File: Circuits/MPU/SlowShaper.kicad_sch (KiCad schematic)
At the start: 34 parts, among them U22 ADA4805-2ARMZ, U23 ADA4805-2ARMZ

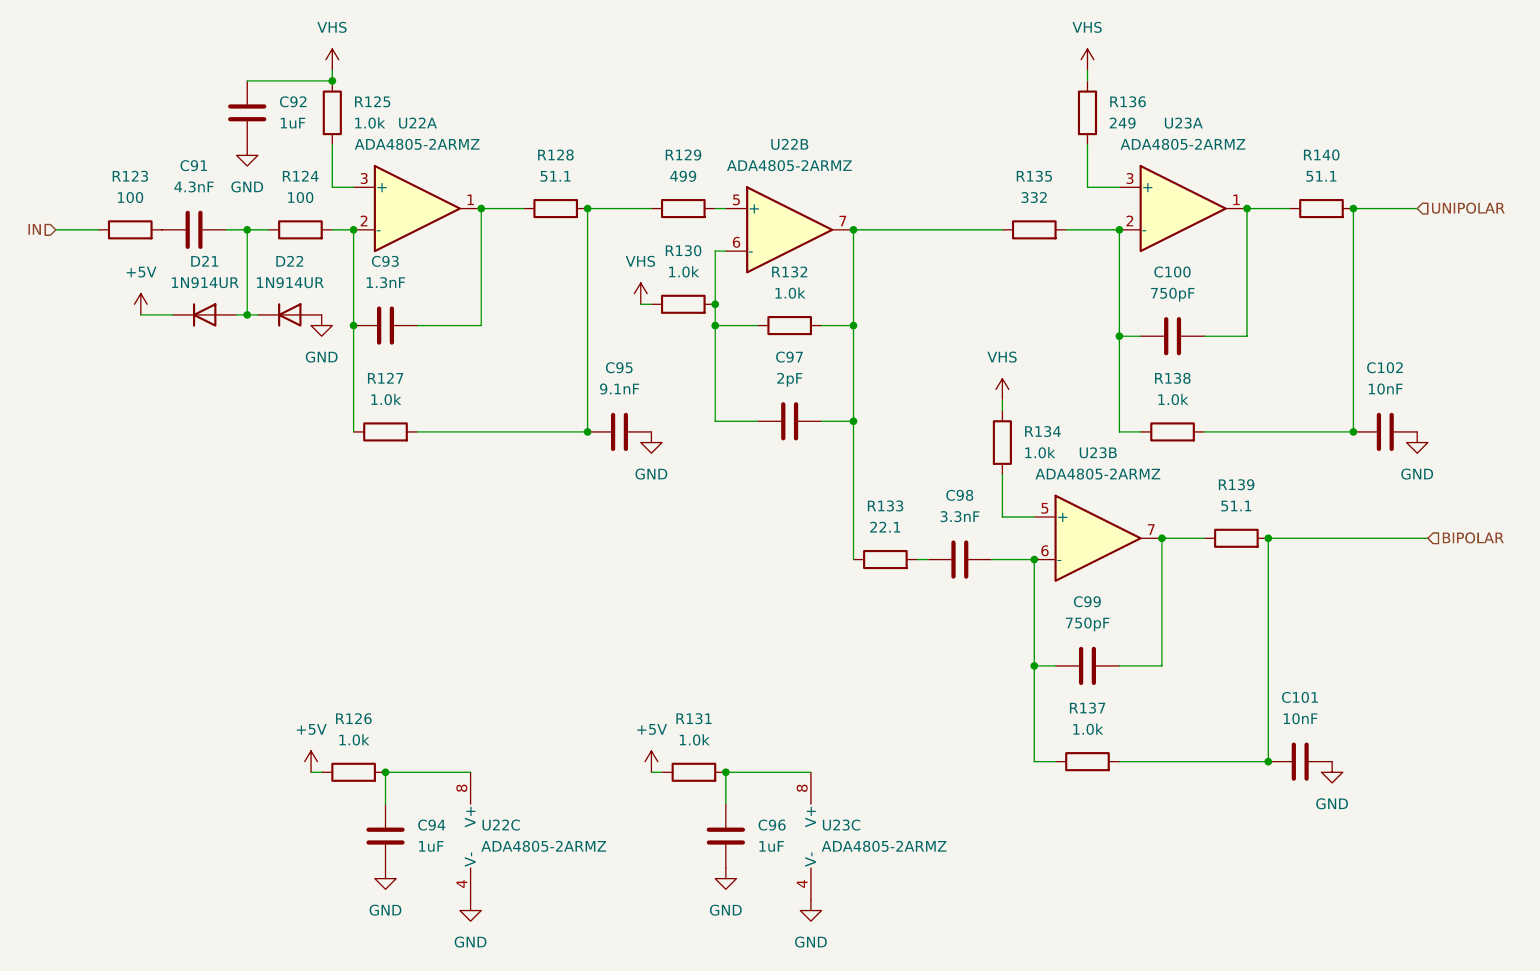
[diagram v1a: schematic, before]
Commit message: PPS is RS422, add MXINH
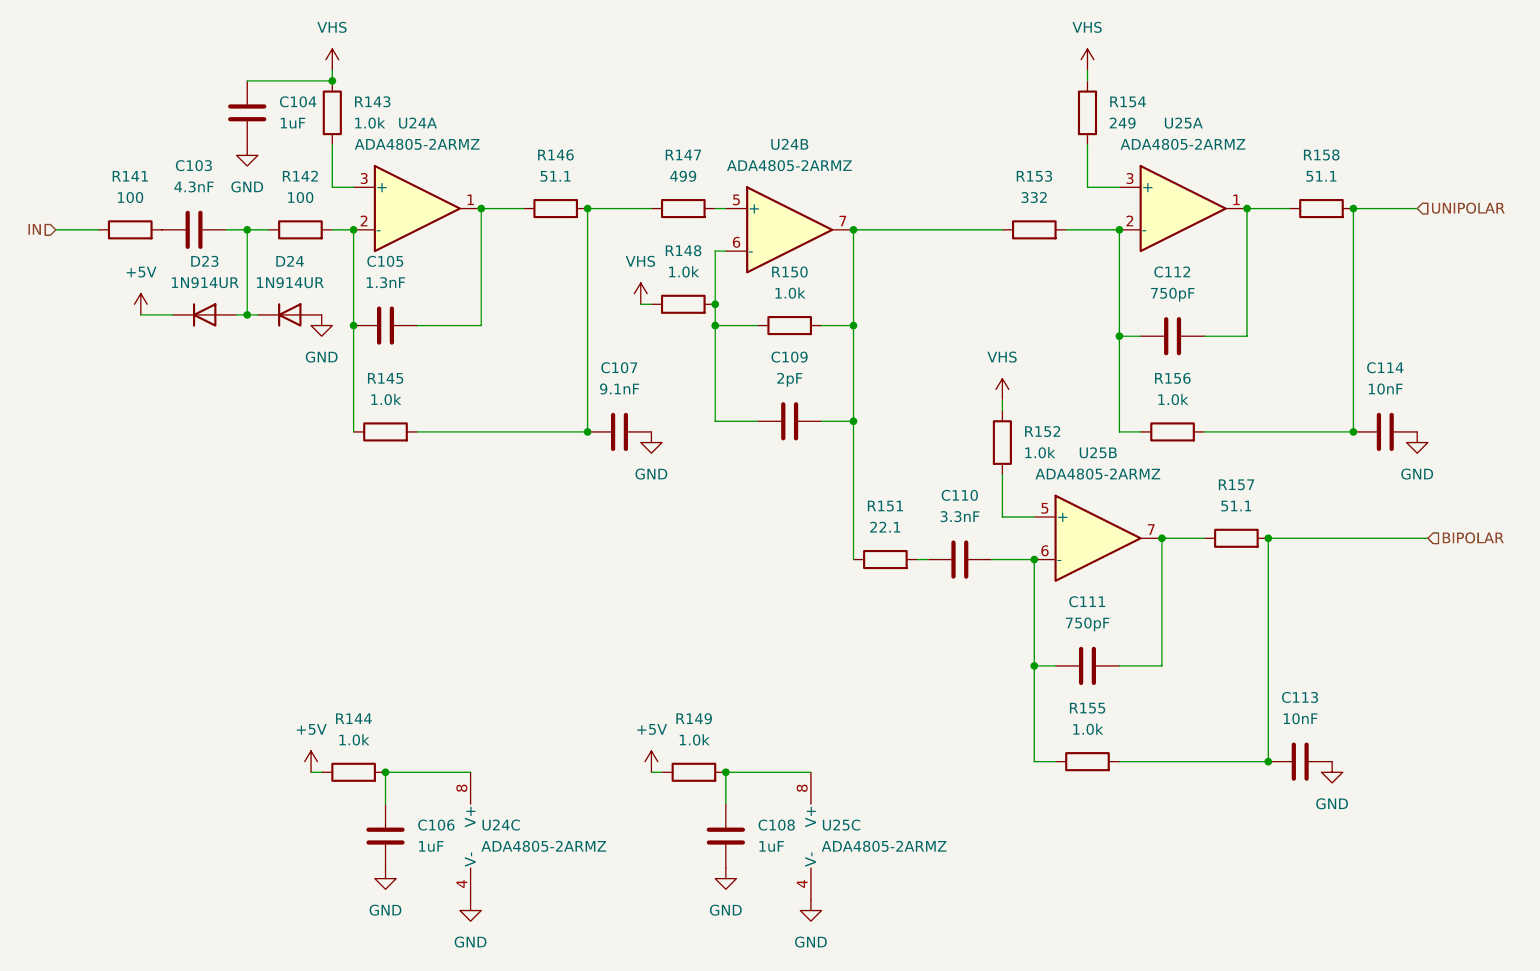
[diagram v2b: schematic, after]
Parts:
- renumbered C91 to C103, C92 to C104, C93 to C105, C94 to C106, C95 to C107, C96 to C108, C97 to C109, C98 to C110, C99 to C111, C100 to C112, C101 to C113, C102 to C114, D21 to D23, D22 to D24, R123 to R141, R124 to R142, R125 to R143, R126 to R144, R127 to R145, R128 to R146, R129 to R147, R130 to R148, R131 to R149, R132 to R150, R133 to R151, R134 to R152, R135 to R153, R136 to R154, R137 to R155, R138 to R156, R139 to R157, R140 to R158, U22 to U24, U23 to U25
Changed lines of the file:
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@@
 	(title_block
 		(title "QuERI MPU")
-		(date "2024-06-05")
-		(rev "RR1")
+		(date "2024-06-27")
+		(rev "RR3")
 		(company "Noqsi Aerospace Ltd")
 		(comment 1 "15 Blanchard Avenue, Billerica MA 01821")
@@
 		(dnp no)
 		(fields_autoplaced yes)
-		(property "Reference" "#PWR0196"
+		(property "Reference" "#PWR0212"
 			(at 52.07 82.55 0)
 			(effects
@@
 		(dnp no)
 		(fields_autoplaced yes)
-		(property "Reference" "C93"
+		(property "Reference" "C105"
 			(at 81.28 72.39 90)
 			(effects
@@
 		(dnp no)
 		(fields_autoplaced yes)
-		(property "Reference" "C92"
+		(property "Reference" "C104"
 			(at 68.58 53.34 0)
 			(effects
@@
 		(dnp no)
 		(fields_autoplaced yes)
-		(property "Reference" "U23"
+		(property "Reference" "U25"
 			(at 166.37 95.25 0)
 			(effects
@@
 		(dnp no)
 		(fields_autoplaced yes)
-		(property "Reference" "#PWR0207"
+		(property "Reference" "#PWR0223"
 			(at 132.08 154.94 0)
 			(effects
@@
 		(dnp no)
 		(fields_autoplaced yes)
-		(property "Reference" "C94"
+		(property "Reference" "C106"
 			(at 85.09 139.7 0)
 			(effects
@@
 		(dnp no)
 		(fields_autoplaced yes)
-		(property "Reference" "#PWR0206"
+		(property "Reference" "#PWR0222"
 			(at 121.92 151.13 0)
 			(effects
@@
 		(dnp no)
 		(fields_autoplaced yes)
-		(property "Reference" "R123"
+		(property "Reference" "R141"
 			(at 50.8 62.23 90)
 			(effects
@@
 		(dnp no)
 		(fields_autoplaced yes)
-		(property "Reference" "R125"
+		(property "Reference" "R143"
 			(at 77.47 53.34 0)
 			(effects
@@
 		(dnp no)
 		(fields_autoplaced yes)
-		(property "Reference" "#PWR0202"
+		(property "Reference" "#PWR0218"
 			(at 91.44 154.94 0)
 			(effects
@@
 		(dnp no)
 		(fields_autoplaced yes)
-		(property "Reference" "R138"
+		(property "Reference" "R156"
 			(at 175.26 86.36 90)
 			(effects
@@
 		(dnp no)
 		(fields_autoplaced yes)
-		(property "Reference" "D22"
+		(property "Reference" "D24"
 			(at 69.85 72.39 0)
 			(effects
@@
 		(dnp no)
 		(fields_autoplaced yes)
-		(property "Reference" "#PWR0200"
+		(property "Reference" "#PWR0216"
 			(at 74.93 53.34 0)
 			(effects
@@
 		(dnp no)
 		(fields_autoplaced yes)
-		(property "Reference" "R140"
+		(property "Reference" "R158"
 			(at 193.04 59.69 90)
 			(effects
@@
 		(dnp no)
 		(fields_autoplaced yes)
-		(property "Reference" "C102"
+		(property "Reference" "C114"
 			(at 200.66 85.09 90)
 			(effects
@@
 		(dnp no)
 		(fields_autoplaced yes)
-		(property "Reference" "R128"
+		(property "Reference" "R146"
 			(at 101.6 59.69 90)
 			(effects
@@
 		(dnp no)
 		(fields_autoplaced yes)
-		(property "Reference" "#PWR0208"
+		(property "Reference" "#PWR0224"
 			(at 154.94 92.71 0)
 			(effects
@@
 		(dnp no)
 		(fields_autoplaced yes)
-		(property "Reference" "C97"
+		(property "Reference" "C109"
 			(at 129.54 83.82 90)
 			(effects
@@
 		(dnp no)
 		(fields_autoplaced yes)
-		(property "Reference" "#PWR0210"
+		(property "Reference" "#PWR0226"
 			(at 194.31 138.43 0)
 			(effects
@@
 		(dnp no)
 		(fields_autoplaced yes)
-		(property "Reference" "C95"
+		(property "Reference" "C107"
 			(at 109.22 85.09 90)
 			(effects
@@
 		(dnp no)
 		(fields_autoplaced yes)
-		(property "Reference" "C99"
+		(property "Reference" "C111"
 			(at 165.1 113.03 90)
 			(effects
@@
 		(dnp no)
 		(fields_autoplaced yes)
-		(property "Reference" "R126"
+		(property "Reference" "R144"
 			(at 77.47 127 90)
 			(effects
@@
 		(dnp no)
 		(fields_autoplaced yes)
-		(property "Reference" "R131"
+		(property "Reference" "R149"
 			(at 118.11 127 90)
 			(effects
@@
 		(dnp no)
 		(fields_autoplaced yes)
-		(property "Reference" "#PWR0205"
+		(property "Reference" "#PWR0221"
 			(at 113.03 137.16 0)
 			(effects
@@
 		(dnp no)
 		(fields_autoplaced yes)
-		(property "Reference" "C101"
+		(property "Reference" "C113"
 			(at 190.5 124.46 90)
 			(effects
@@
 		(dnp no)
 		(fields_autoplaced yes)
-		(property "Reference" "#PWR0203"
+		(property "Reference" "#PWR0219"
 			(at 111.76 81.28 0)
 			(effects
@@
 		(dnp no)
 		(fields_autoplaced yes)
-		(property "Reference" "#PWR0201"
+		(property "Reference" "#PWR0217"
 			(at 81.28 151.13 0)
 			(effects
@@
 		(dnp no)
 		(fields_autoplaced yes)
-		(property "Reference" "C98"
+		(property "Reference" "C110"
 			(at 149.86 100.33 90)
 			(effects
@@
 		(dnp no)
 		(fields_autoplaced yes)
-		(property "Reference" "U22"
+		(property "Reference" "U24"
 			(at 92.71 139.7 0)
 			(effects
@@
 		(dnp no)
 		(fields_autoplaced yes)
-		(property "Reference" "#PWR0209"
+		(property "Reference" "#PWR0225"
 			(at 165.1 53.34 0)
 			(effects
@@
 		(dnp no)
 		(fields_autoplaced yes)
-		(property "Reference" "R124"
+		(property "Reference" "R142"
 			(at 71.12 62.23 90)
 			(effects
@@
 		(dnp no)
 		(fields_autoplaced yes)
-		(property "Reference" "#PWR0211"
+		(property "Reference" "#PWR0227"
 			(at 204.47 99.06 0)
 			(effects
@@
 		(dnp no)
 		(fields_autoplaced yes)
-		(property "Reference" "R137"
+		(property "Reference" "R155"
 			(at 165.1 125.73 90)
 			(effects
@@
 		(dnp no)
 		(fields_autoplaced yes)
-		(property "Reference" "C91"
+		(property "Reference" "C103"
 			(at 58.42 60.96 90)
 			(effects
@@
 		(dnp no)
 		(fields_autoplaced yes)
-		(property "Reference" "C96"
+		(property "Reference" "C108"
 			(at 125.73 139.7 0)
 			(effects
@@
 		(dnp no)
 		(fields_autoplaced yes)
-		(property "Reference" "C100"
+		(property "Reference" "C112"
 			(at 175.26 73.66 90)
 			(effects
@@
 		(dnp no)
 		(fields_autoplaced yes)
-		(property "Reference" "R136"
+		(property "Reference" "R154"
 			(at 167.64 53.3399 0)
 			(effects
@@
 		(dnp no)
 		(fields_autoplaced yes)
-		(property "Reference" "#PWR0199"
+		(property "Reference" "#PWR0215"
 			(at 73.66 85.09 0)
 			(effects
@@
 		(dnp no)
 		(fields_autoplaced yes)
-		(property "Reference" "R127"
+		(property "Reference" "R145"
 			(at 81.28 86.36 90)
 			(effects
@@
 		(dnp no)
 		(fields_autoplaced yes)
-		(property "Reference" "R132"
+		(property "Reference" "R150"
 			(at 129.54 73.66 90)
 			(effects
@@
 		(dnp no)
 		(fields_autoplaced yes)
-		(property "Reference" "R134"
+		(property "Reference" "R152"
 			(at 157.48 92.71 0)
 			(effects
@@
 		(dnp no)
 		(fields_autoplaced yes)
-		(property "Reference" "R135"
+		(property "Reference" "R153"
 			(at 158.75 62.23 90)
 			(effects
@@
 		(dnp no)
 		(fields_autoplaced yes)
-		(property "Reference" "U23"
+		(property "Reference" "U25"
 			(at 133.35 139.7 0)
 			(effects
@@
 		(dnp no)
 		(fields_autoplaced yes)
-		(property "Reference" "R130"
+		(property "Reference" "R148"
 			(at 116.84 71.12 90)
 			(effects
@@
 		(dnp no)
 		(fields_autoplaced yes)
-		(property "Reference" "#PWR0198"
+		(property "Reference" "#PWR0214"
 			(at 72.39 137.16 0)
 			(effects
@@
 		(dnp no)
 		(fields_autoplaced yes)
-		(property "Reference" "#PWR0197"
+		(property "Reference" "#PWR0213"
 			(at 64.77 64.77 0)
 			(effects
@@
 		(dnp no)
 		(fields_autoplaced yes)
-		(property "Reference" "R129"
+		(property "Reference" "R147"
 			(at 116.84 59.69 90)
 			(effects
@@
 		(dnp no)
 		(fields_autoplaced yes)
-		(property "Reference" "U23"
+		(property "Reference" "U25"
 			(at 176.53 55.88 0)
 			(effects
@@
 		(dnp no)
 		(fields_autoplaced yes)
-		(property "Reference" "R133"
+		(property "Reference" "R151"
 			(at 140.97 101.6 90)
 			(effects
@@
 		(dnp no)
 		(fields_autoplaced yes)
-		(property "Reference" "#PWR0204"
+		(property "Reference" "#PWR0220"
 			(at 113.03 99.06 0)
 			(effects
@@
 		(dnp no)
 		(fields_autoplaced yes)
-		(property "Reference" "D21"
+		(property "Reference" "D23"
 			(at 59.69 72.39 0)
 			(effects
@@
 		(dnp no)
 		(fields_autoplaced yes)
-		(property "Reference" "R139"
+		(property "Reference" "R157"
 			(at 182.88 99.06 90)
 			(effects
@@
 		(dnp no)
 		(fields_autoplaced yes)
-		(property "Reference" "U22"
+		(property "Reference" "U24"
 			(at 129.54 58.42 0)
 			(effects
@@
 		(dnp no)
 		(fields_autoplaced yes)
-		(property "Reference" "U22"
+		(property "Reference" "U24"
 			(at 85.09 55.88 0)
 			(effects

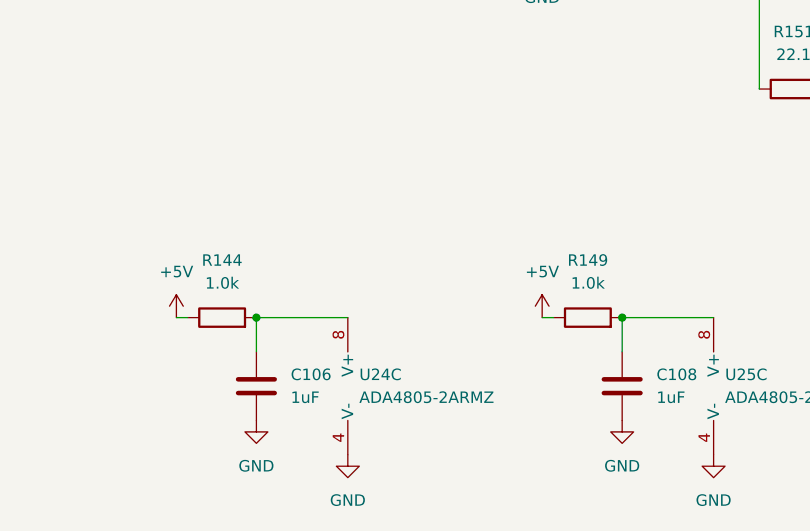
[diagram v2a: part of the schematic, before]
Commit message: Fix errors found by Norm Dobson
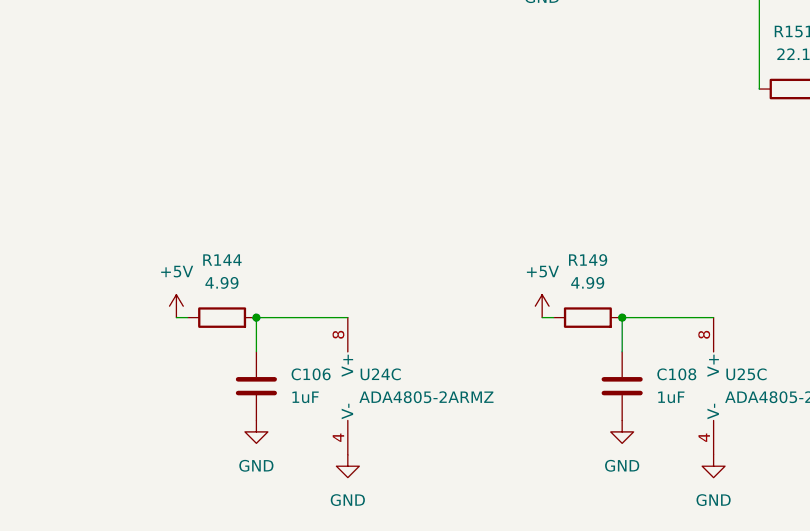
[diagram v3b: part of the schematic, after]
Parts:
- R144, R149: value 1.0k -> 4.99
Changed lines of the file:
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@@
 			)
 		)
-		(property "Value" "1.0k"
+		(property "Value" "4.99"
 			(at 77.47 129.54 90)
 			(effects
@@
 			)
 		)
-		(property "Value" "1.0k"
+		(property "Value" "4.99"
 			(at 118.11 129.54 90)
 			(effects
